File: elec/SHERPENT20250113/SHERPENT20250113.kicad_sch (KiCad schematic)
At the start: 79 parts, among them J1 2137160001, Q1 NMOS, Q2 PMOS, SW1 SW_Push, U1 AN034_ANTENNA, U2 MCP73831T-2ACI_OT, U3 TPS61288LRQQR, U4 TPS7A2633DRVR, U5 LM66200DRLR, U6 ESP32-C3, U7 W25Q128JVS, Y1 40MHz

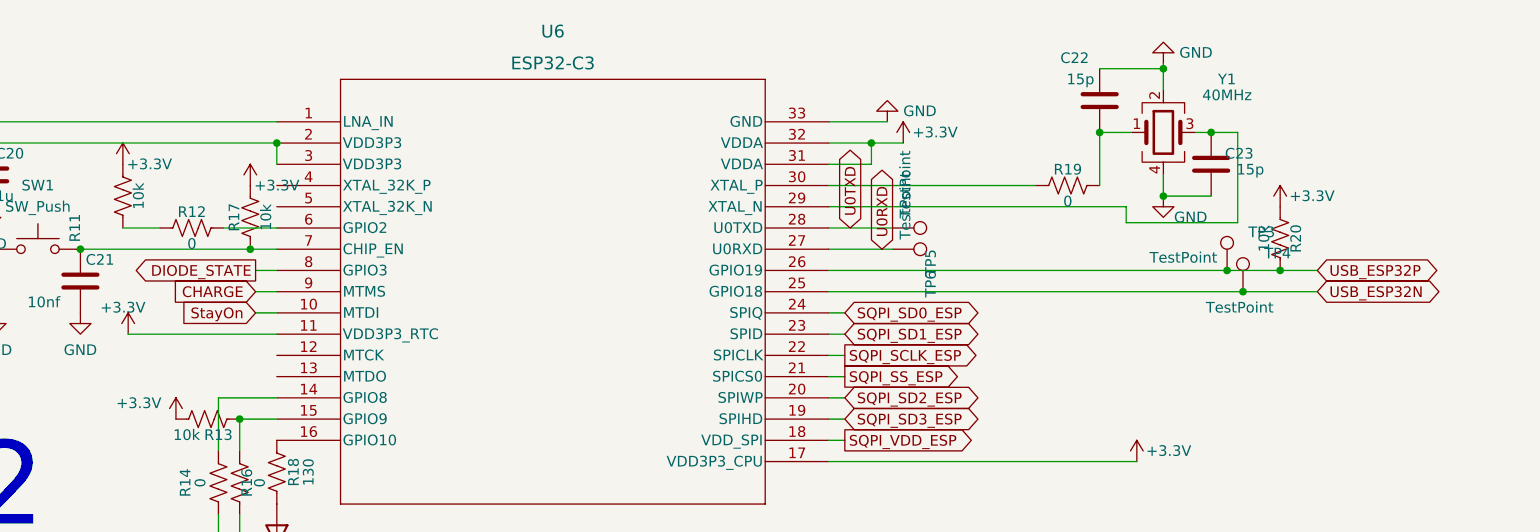
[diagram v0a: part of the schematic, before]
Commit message: Layout: circuit ESP finalisé + début du circuit buck-boost
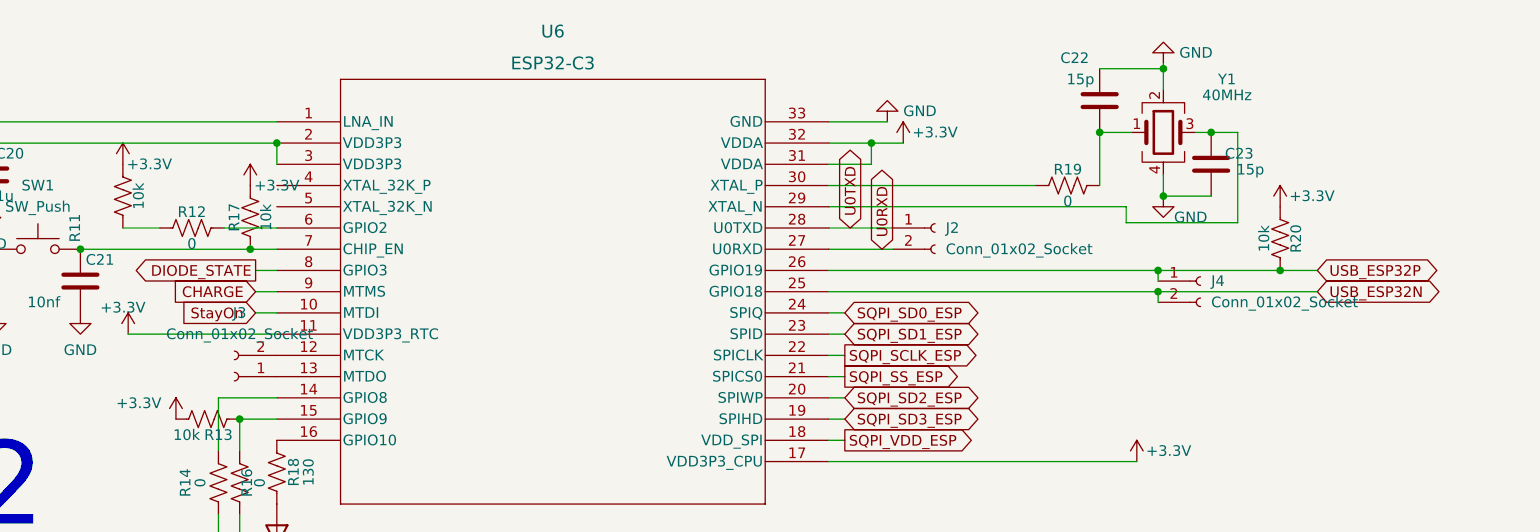
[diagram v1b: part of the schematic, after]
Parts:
- removed TP3, TP4, TP5, TP6: TestPoint, TestPoint:TestPoint_Loop_D2.54mm_Drill1.5mm_Beaded, symbol Connector:TestPoint
- added J2, J3, J4: Conn_01x02_Socket, Connector_PinSocket_2.54mm:PinSocket_1x02_P2.54mm_Vertical, symbol Connector:Conn_01x02_Socket
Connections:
- net U0RXD: now also J2.2 (Pin_2)
- net U0TXD: now also J2.1 (Pin_1)
- net USB_ESP32N: now also J4.2 (Pin_2)
- net USB_ESP32P: now also J4.1 (Pin_1)
- net at U6.12 (MTCK): now also J3.2 (Pin_2)
- net at U6.13 (MTDO): now also J3.1 (Pin_1)

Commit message: Auto stash before merge of "main" and "origin/main"
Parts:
- removed J4: Conn_01x02_Socket, Connector_PinSocket_2.54mm:PinSocket_1x02_P2.54mm_Vertical, symbol Connector:Conn_01x02_Socket
- added D10, D11, D5, D6, D7, D8, D9: WS2812B, LED_SMD:LED_WS2812B_PLCC4_5.0x5.0mm_P3.2mm, symbol LED:WS2812B
- added D12, D13, D14, D15, D16, D17, D18, D19: WS2812B4020, Library:WS2812B4020, symbol WS2812B4020:WS2812B
- added TP10: TestPoint, TestPoint:TestPoint_Pad_D1.5mm, symbol Connector:TestPoint
- added TP4, TP5: TestPoint, TestPoint:TestPoint_Loop_D2.54mm_Drill1.5mm_Beaded, symbol Connector:TestPoint
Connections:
- net GND: now also D11.3 (VSS), D12.4 (VSS), D13.4 (VSS), D14.4 (VSS), D15.4 (VSS), D16.4 (VSS), D17.4 (VSS), D18.4 (VSS), D19.4 (VSS), D5.3 (VSS), D6.3 (VSS), D7.3 (VSS), D8.3 (VSS), D9.3 (VSS)
- net U0TXD: now also TP5.1
- net USB_ESP32N: now also TP4.1; no longer U6.25 (GPIO18)
- new net: D11.2 (DOUT), D12.1 (DIN)
- new net: D12.3 (DOUT), D13.1 (DIN)
- new net: D8.2 (DOUT), D9.4 (DIN)
- new net: D7.2 (DOUT), D8.4 (DIN)
- new net: D6.2 (DOUT), D7.4 (DIN)
- new net: D5.2 (DOUT), D6.4 (DIN)
- new net: D15.3 (DOUT), D16.1 (DIN)
- new net: D16.3 (DOUT), D17.1 (DIN)
- new net: D10.2 (DOUT), D11.4 (DIN)
- new net: D14.3 (DOUT), D15.1 (DIN)
- new net: D10.4 (DIN), D9.2 (DOUT)
- new net: D18.3 (DOUT), D19.1 (DIN)
- new net: D13.3 (DOUT), D14.1 (DIN)
- new net: D19.3 (DOUT), TP10.1
- new net +5V: D10.1 (VDD), D12.2 (VDD), D13.2 (VDD), D14.2 (VDD), D15.2 (VDD), D16.2 (VDD), D17.2 (VDD), D18.2 (VDD), D19.2 (VDD), D5.1 (VDD), D6.1 (VDD), D7.1 (VDD), D8.1 (VDD), D9.1 (VDD)

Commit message: chu pas sur de ce que je fais live
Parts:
- added D4: WS2812B, LED_SMD:LED_WS2812B_PLCC4_5.0x5.0mm_P3.2mm, symbol LED:WS2812B
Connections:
- net +5V: now also D11.1 (VDD), D4.1 (VDD)
- net GND: now also D10.3 (VSS), D4.3 (VSS)
- net NEO: now also D4.4 (DIN)
- net at D17.3 (DOUT): now also D18.1 (DIN)
- net at D5.4 (DIN): now also D4.2 (DOUT)

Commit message: Avancement du circuit des batteries et de contrôle
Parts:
- removed J3: Conn_01x02_Socket, Connector_PinSocket_2.54mm:PinSocket_1x02_P2.54mm_Vertical, symbol Connector:Conn_01x02_Socket
- removed TP5: TestPoint, TestPoint:TestPoint_Loop_D2.54mm_Drill1.5mm_Beaded, symbol Connector:TestPoint
- added D20: D, Diode_SMD:D_0603_1608Metric_Pad1.05x0.95mm_HandSolder, symbol Device:D
- added J3, J4: Conn_01x03_Socket, Connector_PinSocket_2.54mm:PinSocket_1x03_P2.54mm_Vertical, symbol Connector:Conn_01x03_Socket
- added R26: 10k, Resistor_SMD:R_0603_1608Metric, symbol Device:R_US
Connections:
- net +3.3V: now also R22.2
- net +9V: now also D20.2 (A), J3.1 (Pin_1), J4.1 (Pin_1); no longer U5.6 (VIN2)
- net CHARGE: now also R26.1; no longer Q2.1 (D)
- net DIODE_STATE: now also R22.1, U5.8 (ST); no longer C25.1, C9.1, R22.2, TP7.1, U4.4 (EN), U4.6 (IN), U5.2 (VOUT), U5.7 (VOUT)
- net GND: now also J3.3 (Pin_3), J4.3 (Pin_3)
- net USB_ESP32N: now also U6.25 (GPIO18); no longer TP4.1
- net Moteur2_PWM: now reaches U6.13 (MTDO)
- net Moteur2_PWM: now also J4.2 (Pin_2)
- net Moteur1_PWM: now reaches U6.12 (MTCK)
- net Moteur1_PWM: now also J3.2 (Pin_2)
- net U0RXD renamed I2C_DO
- net U0TXD renamed I2C_DI
- new net: D20.1 (K), U5.6 (VIN2)
- new net: Q2.1 (D), R26.2
- new net VDIODE: C25.1, C9.1, TP7.1, U4.4 (EN), U4.6 (IN), U5.2 (VOUT), U5.7 (VOUT)
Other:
- note added: "Connecteur Moteur"
- moved on the sheet: J2

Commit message: Ajout des LED sur le pcb
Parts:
- added R27, R28, R29, R30, R31, R32, R33, R34, R35, R36, R37, R38, R39, R40, R41, R42: 0, Resistor_SMD:R_0603_1608Metric, symbol Device:R_US
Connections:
- net NEO is gone; now on net I2C_DO: D4.4 (DIN)
- net I2C_DI: now also D19.3 (DOUT), TP10.1, R42.1
- net I2C_DO: now also R27.2
- net at D11.2 (DOUT), D12.1 (DIN): now also R34.1, R35.2
- net at D12.3 (DOUT), D13.1 (DIN): now also R35.1, R36.2
- net at D8.2 (DOUT), D9.4 (DIN): now also R31.1, R32.2
- net at D7.2 (DOUT), D8.4 (DIN): now also R30.1, R31.2
- net at D6.2 (DOUT), D7.4 (DIN): now also R29.1, R30.2
- net at D5.2 (DOUT), D6.4 (DIN): now also R28.1, R29.2
- net at D15.3 (DOUT), D16.1 (DIN): now also R38.1, R39.2
- net at D16.3 (DOUT), D17.1 (DIN): now also R39.1, R40.2
- net at D17.3 (DOUT), D18.1 (DIN): now also R40.1, R41.2
- net at D10.2 (DOUT), D11.4 (DIN): now also R33.1, R34.2
- net at D14.3 (DOUT), D15.1 (DIN): now also R37.1, R38.2
- net at D4.2 (DOUT), D5.4 (DIN): now also R27.1, R28.2
- net at D10.4 (DIN), D9.2 (DOUT): now also R32.1, R33.2
- net at D18.3 (DOUT), D19.1 (DIN): now also R41.1, R42.2
- net at D13.3 (DOUT), D14.1 (DIN): now also R36.1, R37.2
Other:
- moved on the sheet: TP10

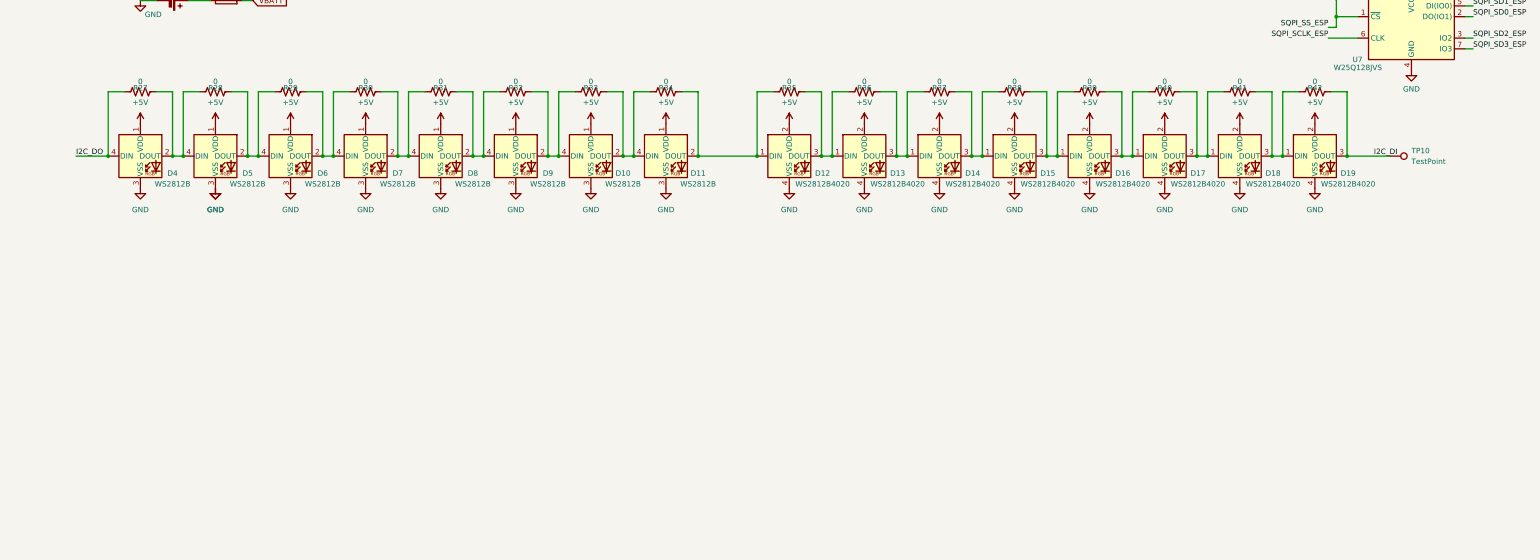
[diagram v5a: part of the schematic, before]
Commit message: rough rgb placement
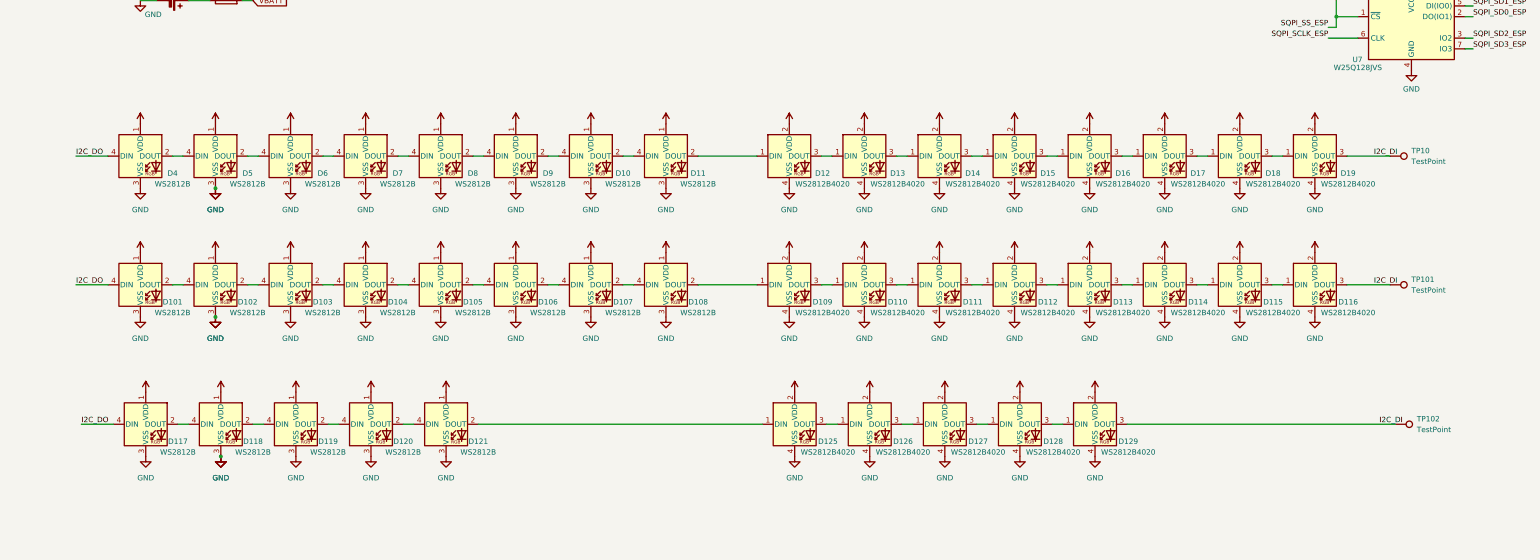
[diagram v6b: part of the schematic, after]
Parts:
- removed R27, R28, R29, R30, R31, R32, R33, R34, R35, R36, R37, R38, R39, R40, R41, R42: 0, Resistor_SMD:R_0603_1608Metric, symbol Device:R_US
- added D101, D102, D103, D104, D105, D106, D107, D108, D117, D118, D119, D120, D121: WS2812B, LED_SMD:LED_WS2812B_PLCC4_5.0x5.0mm_P3.2mm, symbol LED:WS2812B
- added D109, D110, D111, D112, D113, D114, D115, D116, D125, D126, D127, D128, D129: WS2812B4020, Library:WS2812B4020, symbol WS2812B4020:WS2812B
- added TP101, TP102: TestPoint, TestPoint:TestPoint_Pad_D1.5mm, symbol Connector:TestPoint
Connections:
- net +5V: now also D101.1 (VDD), D102.1 (VDD), D103.1 (VDD), D104.1 (VDD), D105.1 (VDD), D106.1 (VDD), D107.1 (VDD), D108.1 (VDD), D109.2 (VDD), D110.2 (VDD), D111.2 (VDD), D112.2 (VDD), D113.2 (VDD), D114.2 (VDD), D115.2 (VDD), D116.2 (VDD), D117.1 (VDD), D118.1 (VDD), D119.1 (VDD), D120.1 (VDD), D121.1 (VDD), D125.2 (VDD), D126.2 (VDD), D127.2 (VDD), D128.2 (VDD), D129.2 (VDD)
- net GND: now also D101.3 (VSS), D102.3 (VSS), D103.3 (VSS), D104.3 (VSS), D105.3 (VSS), D106.3 (VSS), D107.3 (VSS), D108.3 (VSS), D109.4 (VSS), D110.4 (VSS), D111.4 (VSS), D112.4 (VSS), D113.4 (VSS), D114.4 (VSS), D115.4 (VSS), D116.4 (VSS), D117.3 (VSS), D118.3 (VSS), D119.3 (VSS), D120.3 (VSS), D121.3 (VSS), D125.4 (VSS), D126.4 (VSS), D127.4 (VSS), D128.4 (VSS), D129.4 (VSS)
- net I2C_DI: now also D116.3 (DOUT), D129.3 (DOUT), TP101.1, TP102.1
- net I2C_DO: now also D101.4 (DIN), D117.4 (DIN)
- new net: D113.3 (DOUT), D114.1 (DIN)
- new net: D114.3 (DOUT), D115.1 (DIN)
- new net: D108.2 (DOUT), D109.1 (DIN)
- new net: D107.2 (DOUT), D108.4 (DIN)
- new net: D110.3 (DOUT), D111.1 (DIN)
- new net: D111.3 (DOUT), D112.1 (DIN)
- new net: D126.3 (DOUT), D127.1 (DIN)
- new net: D127.3 (DOUT), D128.1 (DIN)
- new net: D121.2 (DOUT), D125.1 (DIN)
- new net: D125.3 (DOUT), D126.1 (DIN)
- new net: D106.2 (DOUT), D107.4 (DIN)
- new net: D105.2 (DOUT), D106.4 (DIN)
- new net: D104.2 (DOUT), D105.4 (DIN)
- new net: D128.3 (DOUT), D129.1 (DIN)
- new net: D115.3 (DOUT), D116.1 (DIN)
- new net: D102.2 (DOUT), D103.4 (DIN)
- new net: D101.2 (DOUT), D102.4 (DIN)
- new net: D109.3 (DOUT), D110.1 (DIN)
- new net: D103.2 (DOUT), D104.4 (DIN)
- new net: D120.2 (DOUT), D121.4 (DIN)
- new net: D119.2 (DOUT), D120.4 (DIN)
- new net: D112.3 (DOUT), D113.1 (DIN)
- new net: D117.2 (DOUT), D118.4 (DIN)
- new net: D118.2 (DOUT), D119.4 (DIN)

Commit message: Quicksave. J'ai mis le connecteur du bon bord. Va falloir flipper le trou de place pis recheck le routing. Stayon circuit en cours
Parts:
- added D122, D123: D_Schottky, LED_SMD:LED_0603_1608Metric_Pad1.05x0.95mm_HandSolder, symbol Device:D_Schottky
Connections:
- net StayOn: now also D122.2 (A); no longer Q1.2 (G), R10.1
- new net: D122.1 (K), D123.1 (K), Q1.2 (G), R10.1
- new net Button: D123.2 (A)
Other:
- moved on the sheet: C1, C10, C11, C12, C2, C25, C3, C4, C5, C6, C7, C9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

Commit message: StayOn supposé être fonctionnel
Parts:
- removed D123: D_Schottky, LED_SMD:LED_0603_1608Metric_Pad1.05x0.95mm_HandSolder, symbol Device:D_Schottky
- removed R10: 10k, Resistor_SMD:R_0603_1608Metric, symbol Device:R_US
- removed R23, R25, R4: 0, Resistor_SMD:R_0603_1608Metric, symbol Device:R_US
- added Q101: PMOS, Package_TO_SOT_SMD:SOT-23, symbol Simulation_SPICE:PMOS
- added R101, R102, R103: 10k, Resistor_SMD:R_0603_1608Metric, symbol Device:R_US
- added SW101: SW_Push, CS1213AGF160:SW_CS1213AG_CRS, symbol Switch:SW_Push
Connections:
- net Button: now also D122.1 (K), R103.2, SW101.2
- net GND: now also R24.2, U3.3 (PGND), R101.2, SW101.1
- net StayOn: now also Q1.2 (G), R101.1; no longer D122.2 (A)
- net VBATT: now also Q101.3 (S), R102.1, R103.1; no longer R24.1
- net at Q1.1 (D): now also D122.2 (A), Q101.2 (G), R102.2
- net at U3.6 (EN): now also R24.1, Q101.1 (D); no longer R24.2
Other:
- note added: "!! Placer Button sur un GPIO !!"
- note added: "←Output←"
- note added: "→Input→"
- moved on the sheet: C1, C2, C3, C4, C5, C6, C7, L1, Q1, R1, R2, R24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
